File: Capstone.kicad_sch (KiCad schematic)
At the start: 4 parts, among them J2 Conn_01x08_Socket, U1 ESP32-C3-WROOM-02, U11 SN74HC161DR, U3 74LS151

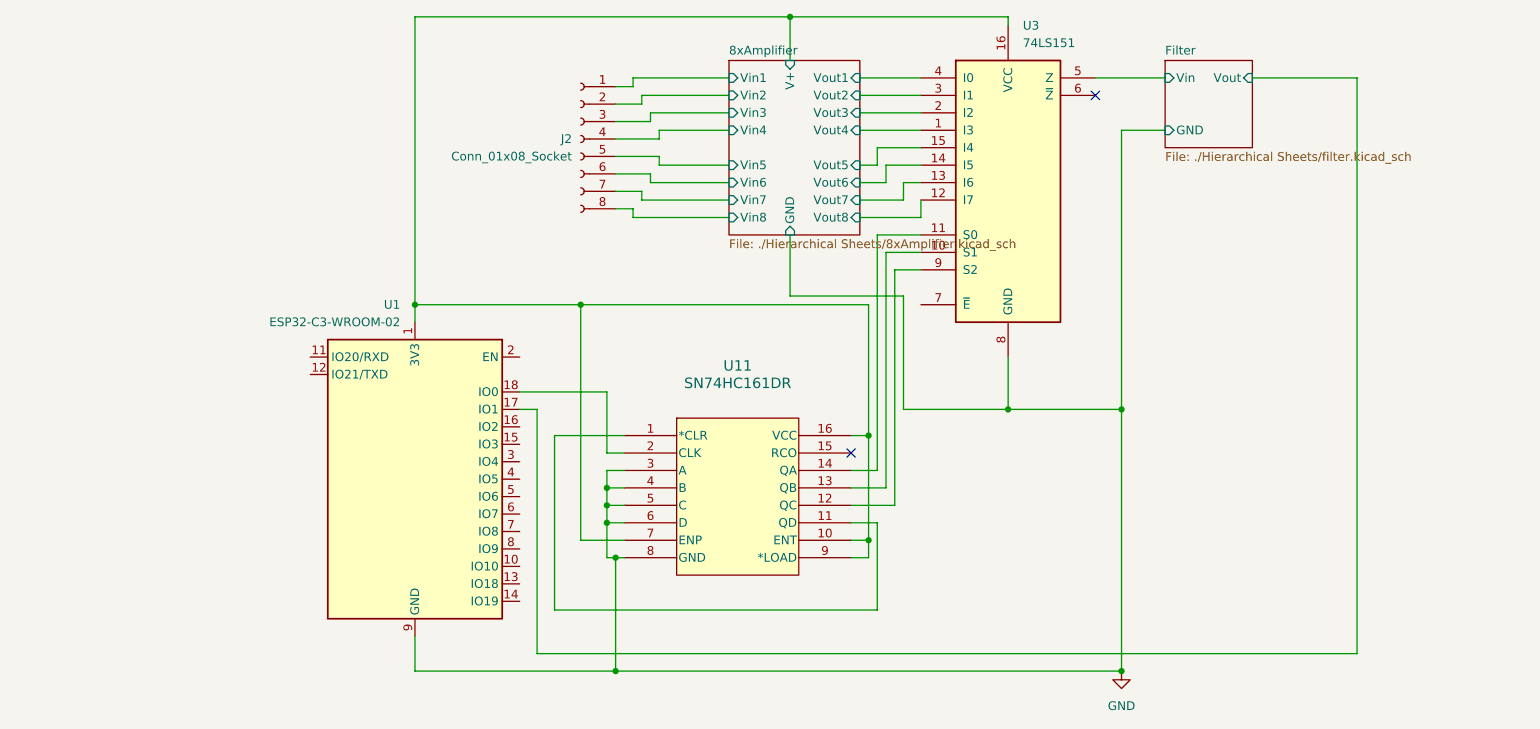
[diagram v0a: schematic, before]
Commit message: Added New Libraries
ESP32 Library - Footprint & Schematics
Binary Counter Footrprint Added
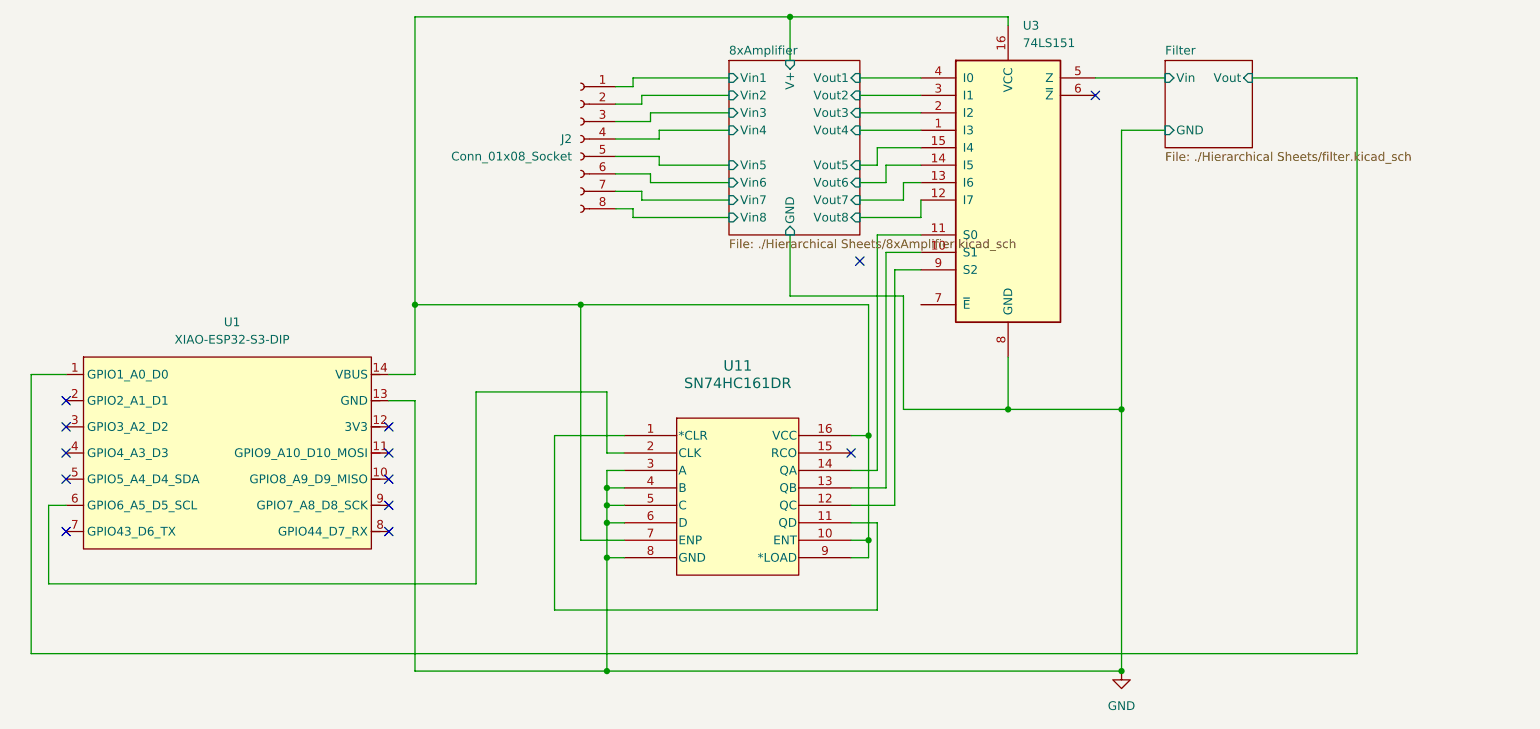
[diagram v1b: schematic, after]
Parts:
- removed U1: ESP32-C3-WROOM-02, RF_Module:ESP32-C3-WROOM-02, symbol RF_Module:ESP32-C3-WROOM-02
- added U1: XIAO-ESP32-S3-DIP, Seeed_Studio_XIAO_Series:XIAO-ESP32-S3-DIP, symbol Seeed_Studio_XIAO_Series:XIAO-ESP32-S3-DIP
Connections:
- net 8xAmplifier/V+: now also U1.14 (VBUS)
- net Filter/Vout: now also U1.1 (GPIO1_A0_D0)
- net GND: now also U1.13 (GND)
- net at U11.2 (CLK): now also U1.6 (GPIO6_A5_D5_SCL)
- no-connect marks 2 -> 13

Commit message: Update .gitignore update PCB footprints
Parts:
- U11: footprint D16 -> CapstoneFootprints:D16
- U3: footprint Package_SO:SOIC-16W_5.3x10.2mm_P1.27mm -> CapstoneFootprints:D16
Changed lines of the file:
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@@
 			)
 		)
-		(property "Footprint" "Package_SO:SOIC-16W_5.3x10.2mm_P1.27mm"
+		(property "Footprint" "CapstoneFootprints:D16"
 			(at 167.64 43.18 0)
 			(effects
@@
 			)
 		)
-		(property "Footprint" "D16"
+		(property "Footprint" "CapstoneFootprints:D16"
 			(at 111.76 80.01 0)
 			(effects

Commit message: Update Root
Working on simulations
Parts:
- U1: footprint Seeed_Studio_XIAO_Series:XIAO-ESP32-S3-DIP -> CapstoneFootprints:XIAO-ESP32-S3-DIP
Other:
- moved on the sheet: U1
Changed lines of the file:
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@@
 	)
 	(no_connect
-		(at 30.48 78.74)
+		(at 29.21 87.63)
 	)
 	(no_connect
-		(at 30.48 74.93)
+		(at 29.21 83.82)
 	)
 	(no_connect
-		(at 77.47 93.98)
+		(at 76.2 102.87)
 	)
 	(no_connect
@@
 	)
 	(no_connect
-		(at 30.48 86.36)
+		(at 29.21 95.25)
 	)
 	(no_connect
-		(at 77.47 86.36)
+		(at 76.2 95.25)
 	)
 	(no_connect
-		(at 30.48 82.55)
+		(at 29.21 91.44)
 	)
 	(no_connect
-		(at 77.47 90.17)
+		(at 76.2 99.06)
 	)
 	(no_connect
-		(at 77.47 78.74)
+		(at 76.2 87.63)
 	)
 	(no_connect
@@
 	)
 	(no_connect
-		(at 77.47 82.55)
+		(at 76.2 91.44)
 	)
 	(no_connect
-		(at 30.48 93.98)
-	)
-	(wire
-		(pts
-			(xy 77.47 74.93) (xy 81.28 74.93)
+		(at 29.21 102.87)
+	)
+	(wire
+		(pts
+			(xy 76.2 83.82) (xy 81.28 83.82)
 		)
 		(stroke
@@
 	(wire
 		(pts
-			(xy 81.28 74.93) (xy 81.28 114.3)
+			(xy 81.28 83.82) (xy 81.28 114.3)
 		)
 		(stroke
@@
 	(wire
 		(pts
-			(xy 90.17 73.66) (xy 109.22 73.66)
+			(xy 90.17 82.55) (xy 111.76 82.55)
 		)
 		(stroke
@@
 	(wire
 		(pts
-			(xy 90.17 101.6) (xy 90.17 73.66)
+			(xy 90.17 109.22) (xy 90.17 82.55)
 		)
 		(stroke
@@
 	(wire
 		(pts
-			(xy 30.48 90.17) (xy 27.94 90.17)
-		)
-		(stroke
-			(width 0)
-			(type default)
-		)
-	)
-	(wire
-		(pts
-			(xy 27.94 90.17) (xy 27.94 101.6)
+			(xy 29.21 99.06) (xy 27.94 99.06)
+		)
+		(stroke
+			(width 0)
+			(type default)
+		)
+	)
+	(wire
+		(pts
+			(xy 27.94 99.06) (xy 27.94 109.22)
 		)
 		(stroke
@@
 	(wire
 		(pts
-			(xy 25.4 71.12) (xy 30.48 71.12)
-		)
-		(stroke
-			(width 0)
-			(type default)
-		)
-	)
-	(wire
-		(pts
-			(xy 25.4 111.76) (xy 25.4 71.12)
+			(xy 25.4 80.01) (xy 29.21 80.01)
+		)
+		(stroke
+			(width 0)
+			(type default)
+		)
+	)
+	(wire
+		(pts
+			(xy 25.4 111.76) (xy 25.4 80.01)
 		)
 		(stroke
@@
 	(wire
 		(pts
-			(xy 81.28 71.12) (xy 81.28 60.96)
+			(xy 81.28 80.01) (xy 81.28 60.96)
 		)
 		(stroke
@@
 	(wire
 		(pts
-			(xy 27.94 101.6) (xy 90.17 101.6)
+			(xy 27.94 109.22) (xy 90.17 109.22)
 		)
 		(stroke
@@
 	(wire
 		(pts
-			(xy 109.22 82.55) (xy 109.22 73.66)
-		)
-		(stroke
-			(width 0)
-			(type default)
-		)
-	)
-	(wire
-		(pts
 			(xy 149.86 43.18) (xy 149.86 40.64)
 		)
@@
 	(wire
 		(pts
-			(xy 111.76 82.55) (xy 109.22 82.55)
-		)
-		(stroke
-			(width 0)
-			(type default)
-		)
-	)
-	(wire
-		(pts
 			(xy 115.57 43.18) (xy 127 43.18)
 		)
@@
 	(wire
 		(pts
-			(xy 77.47 71.12) (xy 81.28 71.12)
+			(xy 76.2 80.01) (xy 81.28 80.01)
 		)
 		(stroke
@@
 	(symbol
 		(lib_id "Seeed_Studio_XIAO_Series:XIAO-ESP32-S3-DIP")
-		(at 33.02 66.04 0)
+		(at 31.75 74.93 0)
 		(unit 1)
-		(exclude_from_sim no)
+		(exclude_from_sim yes)
 		(in_bom yes)
 		(on_board yes)
@@
 		(fields_autoplaced yes)
 		(property "Reference" "U1"
-			(at 54.6481 63.5 0)
+			(at 53.3781 72.39 0)
 			(effects
 				(font
@@
 		)
 		(property "Value" "XIAO-ESP32-S3-DIP"
-			(at 54.6481 66.04 0)
-			(effects
-				(font
-					(size 1.27 1.27)
-				)
-			)
-		)
-		(property "Footprint" "Seeed_Studio_XIAO_Series:XIAO-ESP32-S3-DIP"
-			(at 50.038 97.79 0)
+			(at 53.3781 74.93 0)
+			(effects
+				(font
+					(size 1.27 1.27)
+				)
+			)
+		)
+		(property "Footprint" "CapstoneFootprints:XIAO-ESP32-S3-DIP"
+			(at 48.768 106.68 0)
 			(effects
 				(font
@@
 		)
 		(property "Datasheet" ""
-			(at 33.02 66.04 0)
+			(at 31.75 74.93 0)
 			(effects
 				(font
@@
 		)
 		(property "Description" ""
-			(at 33.02 66.04 0)
+			(at 31.75 74.93 0)
 			(effects
 				(font
@@
 			(at 111.76 80.01 0)
 			(effects
+				(font
+					(size 1.27 1.27)
+				)
+				(hide yes)
+			)
+		)
+		(property "Sim.Library" ".\\"
+			(at 111.76 80.01 0)
+			(effects

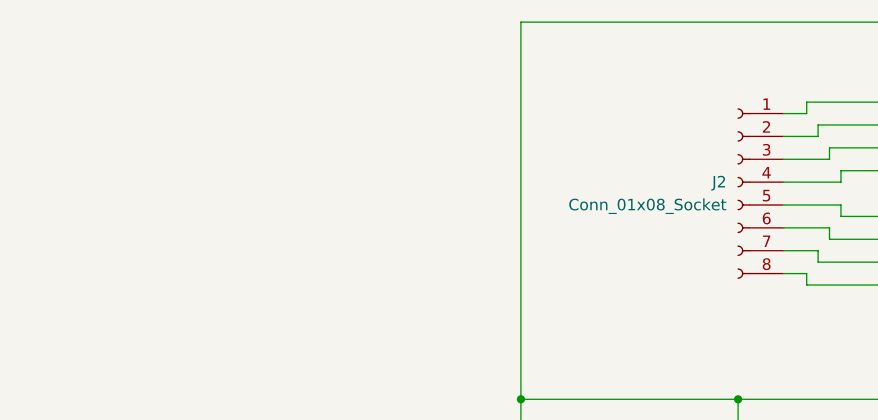
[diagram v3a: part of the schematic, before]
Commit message: Link Battery Charger
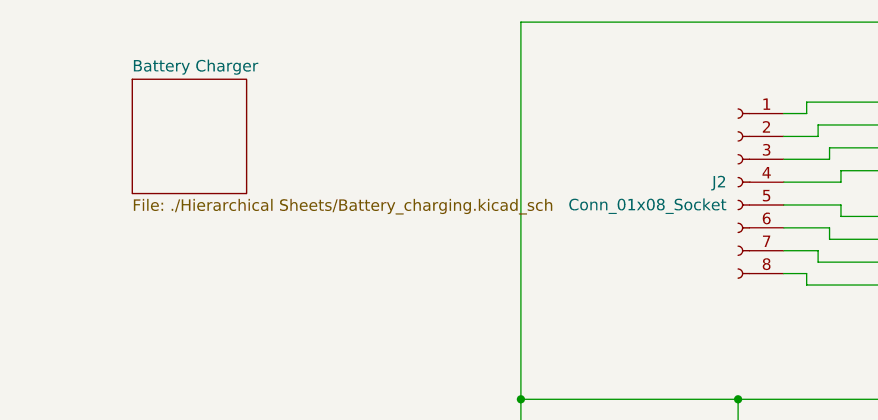
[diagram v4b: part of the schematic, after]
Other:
- added sheet Battery Charger (./Hierarchical Sheets/Battery_charging.kicad_sch)
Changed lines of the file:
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@@
+		)
+	)
+	(sheet
+		(at 38.1 25.4)
+		(size 12.7 12.7)
+		(exclude_from_sim no)
+		(in_bom yes)
+		(on_board yes)
+		(dnp no)
+		(fields_autoplaced yes)
+		(stroke
+			(width 0.1524)
+			(type solid)
+		)
+		(fill
+			(color 0 0 0 0.0000)
+		)
+		(property "Sheetname" "Battery Charger"
+			(at 38.1 24.6884 0)
+			(effects
+				(font
+					(size 1.27 1.27)
+				)
+				(justify left bottom)
+			)
+		)
+		(property "Sheetfile" "./Hierarchical Sheets/Battery_charging.kicad_sch"
+			(at 38.1 38.6846 0)
+			(effects
+				(font
+					(size 1.27 1.27)
+				)
+				(justify left top)
+			)
+		)
+		(instances
+			(project "Capstone"
+				(path "/eb20fb8b-6e33-462b-9505-401dab49dd09"
+					(page "12")
+				)
+			)
 		)
 	)

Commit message: Redo Base Project file add code
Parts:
- removed J2: Conn_01x08_Socket, symbol Connector:Conn_01x08_Socket
- removed U11: SN74HC161DR, CapstoneFootprints:D16, symbol Capstone:SN74HC161DR
- removed U3: 74LS151, CapstoneFootprints:D16, symbol 74xx:74LS151
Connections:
- net SensorReader1/Vout: now reaches U1.2 (GPIO2_A1_D1)
- net 8xAmplifier/V+ renamed SensorReader/V+
- net Filter/Vout renamed SensorReader/Vout
- net GND renamed SensorReader/GND
- no-connect marks 13 -> 10
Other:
- removed sheet 8xAmplifier
- removed sheet Filter
- added sheet SensorReader (Hierarchical Sheets/capSensorReader.kicad_sch)
- added sheet SensorReader1 (Hierarchical Sheets/capSensorReader.kicad_sch)
- note added: "Shear Force Sensors"

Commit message: Update Main Sub Sheets
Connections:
- net SensorReader/GND: no longer names the net of U1.13 (GND)
- net SensorReader/V+: no longer names the net of U1.14 (VBUS)
- net SensorReader/Vout: no longer names the net of U1.1 (GPIO1_A0_D0)
- net SensorReader1/Vout: no longer names the net of U1.2 (GPIO2_A1_D1)
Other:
- removed sheet SensorReader1
- sheet SensorReader ports: added none; removed GND, V+, V-, Vout, Vsin
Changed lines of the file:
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@@
-	)
-	(sheet
-		(at 114.3 50.8)
-		(size 12.7 12.7)
-		(exclude_from_sim no)
-		(in_bom yes)
-		(on_board yes)
-		(dnp no)
-		(fields_autoplaced yes)
-		(stroke
-			(width 0.1524)
-			(type solid)
-		)
-		(fill
-			(color 0 0 0 0.0000)
-		)
-		(property "Sheetname" "SensorReader1"
-			(at 114.3 50.0884 0)
-			(effects
-				(font
-					(size 1.27 1.27)
-				)
-				(justify left bottom)
-			)
-		)
-		(property "Sheetfile" "Hierarchical Sheets/capSensorReader.kicad_sch"
-			(at 114.3 64.0846 0)
-			(effects
-				(font
-					(size 1.27 1.27)
-				)
-				(justify left top)
-			)
-		)
-		(pin "GND" input
-			(at 120.65 63.5 270)
-			(effects
-				(font
-					(size 1.27 1.27)
-				)
-				(justify left)
-			)
-		)
-		(pin "V+" input
-			(at 114.3 60.96 180)
-			(effects
-				(font
-					(size 1.27 1.27)
-				)
-				(justify left)
-			)
-		)
-		(pin "V-" input
-			(at 114.3 53.34 180)
-			(effects
-				(font
-					(size 1.27 1.27)
-				)
-				(justify left)
-			)
-		)
-		(pin "Vout" input
-			(at 127 57.15 0)
-			(effects
-				(font
-					(size 1.27 1.27)
-				)
-				(justify right)
-			)
-		)
-		(pin "Vsin" input
-			(at 114.3 57.15 180)
-			(effects
-				(font
-					(size 1.27 1.27)
-				)
-				(justify left)
-			)
-		)
-		(instances
-			(project "Capstone"
-				(path "/eb20fb8b-6e33-462b-9505-401dab49dd09"
-					(page "2")
-				)
-			)
-		)
 	)
 	(sheet
@@
 			)
 		)
-		(pin "GND" input
-			(at 120.65 38.1 270)
-			(effects
-				(font
-					(size 1.27 1.27)
-				)
-				(justify left)
-			)
-		)
-		(pin "V+" input
-			(at 114.3 35.56 180)
-			(effects
-				(font
-					(size 1.27 1.27)
-				)
-				(justify left)
-			)
-		)
-		(pin "V-" input
-			(at 114.3 27.94 180)
-			(effects
-				(font
-					(size 1.27 1.27)
-				)
-				(justify left)
-			)
-		)
-		(pin "Vout" input
-			(at 127 31.75 0)
-			(effects
-				(font
-					(size 1.27 1.27)
-				)
-				(justify right)
-			)
-		)
-		(pin "Vsin" input
-			(at 114.3 31.75 180)
-			(effects
-				(font
-					(size 1.27 1.27)
-				)
-				(justify left)
-			)
-		)

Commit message: Main Update
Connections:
- net SensorReader/Vout: now reaches U1.1 (GPIO1_A0_D0)
- net SensorReader/GND: now reaches U1.13 (GND)
- net SensorReader/V+: now reaches U1.14 (VBUS)
- net SensorReader1/Vout: now reaches U1.2 (GPIO2_A1_D1)
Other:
- added sheet SensorReader1 (Hierarchical Sheets/capSensorReader.kicad_sch)
- sheet SensorReader ports: added GND, V+, V-, Vout, Vsin; removed none
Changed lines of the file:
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@@
+	)
+	(sheet
+		(at 114.3 50.8)
+		(size 12.7 12.7)
+		(exclude_from_sim no)
+		(in_bom yes)
+		(on_board yes)
+		(dnp no)
+		(fields_autoplaced yes)
+		(stroke
+			(width 0.1524)
+			(type solid)
+		)
+		(fill
+			(color 0 0 0 0.0000)
+		)
+		(property "Sheetname" "SensorReader1"
+			(at 114.3 50.0884 0)
+			(effects
+				(font
+					(size 1.27 1.27)
+				)
+				(justify left bottom)
+			)
+		)
+		(property "Sheetfile" "Hierarchical Sheets/capSensorReader.kicad_sch"
+			(at 114.3 64.0846 0)
+			(effects
+				(font
+					(size 1.27 1.27)
+				)
+				(justify left top)
+			)
+		)
+		(pin "GND" input
+			(at 120.65 63.5 270)
+			(effects
+				(font
+					(size 1.27 1.27)
+				)
+				(justify left)
+			)
+		)
+		(pin "V+" input
+			(at 114.3 60.96 180)
+			(effects
+				(font
+					(size 1.27 1.27)
+				)
+				(justify left)
+			)
+		)
+		(pin "V-" input
+			(at 114.3 53.34 180)
+			(effects
+				(font
+					(size 1.27 1.27)
+				)
+				(justify left)
+			)
+		)
+		(pin "Vsin" input
+			(at 114.3 57.15 180)
+			(effects
+				(font
+					(size 1.27 1.27)
+				)
+				(justify left)
+			)
+		)
+		(pin "Vout" input
+			(at 127 57.15 0)
+			(effects
+				(font
+					(size 1.27 1.27)
+				)
+				(justify right)
+			)
+		)
+		(instances
+			(project "Capstone"
+				(path "/eb20fb8b-6e33-462b-9505-401dab49dd09"
+					(page "2")
+				)
+			)
+		)
 	)
 	(sheet
@@
 			)
 		)
+		(pin "GND" input
+			(at 120.65 38.1 270)
+			(effects
+				(font
+					(size 1.27 1.27)
+				)
+				(justify left)
+			)
+		)
+		(pin "V+" input
+			(at 114.3 35.56 180)
+			(effects
+				(font
+					(size 1.27 1.27)
+				)
+				(justify left)
+			)
+		)
+		(pin "V-" input
+			(at 114.3 27.94 180)
+			(effects
+				(font
+					(size 1.27 1.27)
+				)
+				(justify left)
+			)
+		)
+		(pin "Vsin" input
+			(at 114.3 31.75 180)
+			(effects
+				(font
+					(size 1.27 1.27)
+				)
+				(justify left)
+			)
+		)
+		(pin "Vout" input
+			(at 127 31.75 0)
+			(effects
+				(font
+					(size 1.27 1.27)
+				)
+				(justify right)
+			)
+		)

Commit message: PCB designed rev1.0
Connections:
- net SensorReader/GND renamed Battery Charger/GND
- net SensorReader/V+ renamed Battery Charger/5V
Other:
- sheet Battery Charger ports: added -5V, 5V, GND; removed none
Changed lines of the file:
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@@
+	)
+	(junction
+		(at 104.14 27.94)
+		(diameter 0)
+		(color 0 0 0 0)
 	)
 	(junction
@@
 	)
 	(junction
+		(at 81.28 80.01)
+		(diameter 0)
+		(color 0 0 0 0)
+	)
+	(junction
 		(at 109.22 66.04)
 		(diameter 0)
@@
 	(wire
 		(pts
+			(xy 38.1 31.75) (xy 27.94 31.75)
+		)
+		(stroke
+			(width 0)
+			(type default)
+		)
+	)
+	(wire
+		(pts
 			(xy 104.14 53.34) (xy 104.14 27.94)
 		)
@@
 	(wire
 		(pts
+			(xy 81.28 80.01) (xy 81.28 27.94)
+		)
+		(stroke
+			(width 0)
+			(type default)
+		)
+	)
+	(wire
+		(pts
+			(xy 81.28 27.94) (xy 50.8 27.94)
+		)
+		(stroke
+			(width 0)
+			(type default)
+		)
+	)
+	(wire
+		(pts
 			(xy 120.65 38.1) (xy 120.65 40.64)
 		)
@@
 	(wire
 		(pts
+			(xy 93.98 35.56) (xy 93.98 27.94)
+		)
+		(stroke
+			(width 0)
+			(type default)
+		)
+	)
+	(wire
+		(pts
 			(xy 109.22 40.64) (xy 109.22 66.04)
 		)
@@
 	(wire
 		(pts
+			(xy 50.8 35.56) (xy 93.98 35.56)
+		)
+		(stroke
+			(width 0)
+			(type default)
+		)
+	)
+	(wire
+		(pts
 			(xy 120.65 63.5) (xy 120.65 66.04)
 		)
@@
 	(wire
 		(pts
+			(xy 81.28 80.01) (xy 106.68 80.01)
+		)
+		(stroke
+			(width 0)
+			(type default)
+		)
+	)
+	(wire
+		(pts
 			(xy 106.68 60.96) (xy 106.68 35.56)
 		)
@@
 	(wire
 		(pts
+			(xy 93.98 27.94) (xy 104.14 27.94)
+		)
+		(stroke
+			(width 0)
+			(type default)
+		)
+	)
+	(wire
+		(pts
+			(xy 27.94 66.04) (xy 109.22 66.04)
+		)
+		(stroke
+			(width 0)
+			(type default)
+		)
+	)
+	(wire
+		(pts
 			(xy 120.65 40.64) (xy 109.22 40.64)
 		)
@@
 	(wire
 		(pts
-			(xy 76.2 80.01) (xy 106.68 80.01)
+			(xy 76.2 80.01) (xy 81.28 80.01)
 		)
 		(stroke
@@
 		(pts
 			(xy 25.4 114.3) (xy 25.4 83.82)
+		)
+		(stroke
+			(width 0)
+			(type default)
+		)
+	)
+	(wire
+		(pts
+			(xy 27.94 31.75) (xy 27.94 66.04)
 		)
 		(stroke
@@
 		(at 38.1 25.4)
 		(size 12.7 12.7)
-		(exclude_from_sim yes)
-		(in_bom no)
-		(on_board no)
+		(exclude_from_sim no)
+		(in_bom yes)
+		(on_board yes)
 		(dnp no)
 		(fields_autoplaced yes)
@@
 			)
 		)
+		(pin "-5V" input
+			(at 50.8 35.56 0)
+			(effects
+				(font
+					(size 1.27 1.27)
+				)
+				(justify right)
+			)
+		)
+		(pin "5V" input
+			(at 50.8 27.94 0)
+			(effects
+				(font
+					(size 1.27 1.27)
+				)
+				(justify right)
+			)
+		)
+		(pin "GND" input
+			(at 38.1 31.75 180)
+			(effects
+				(font
+					(size 1.27 1.27)
+				)
+				(justify left)
+			)
+		)
